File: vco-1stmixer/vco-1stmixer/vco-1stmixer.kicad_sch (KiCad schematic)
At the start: 51 parts, among them J101 VCO Control In, J102 1st IF Out, J103 VCO Sample, J104 RF In, J105 Conn_01x02, U101 POS-200, U102 MAV-11, U103 MAV-11, U104 TUF-1H+

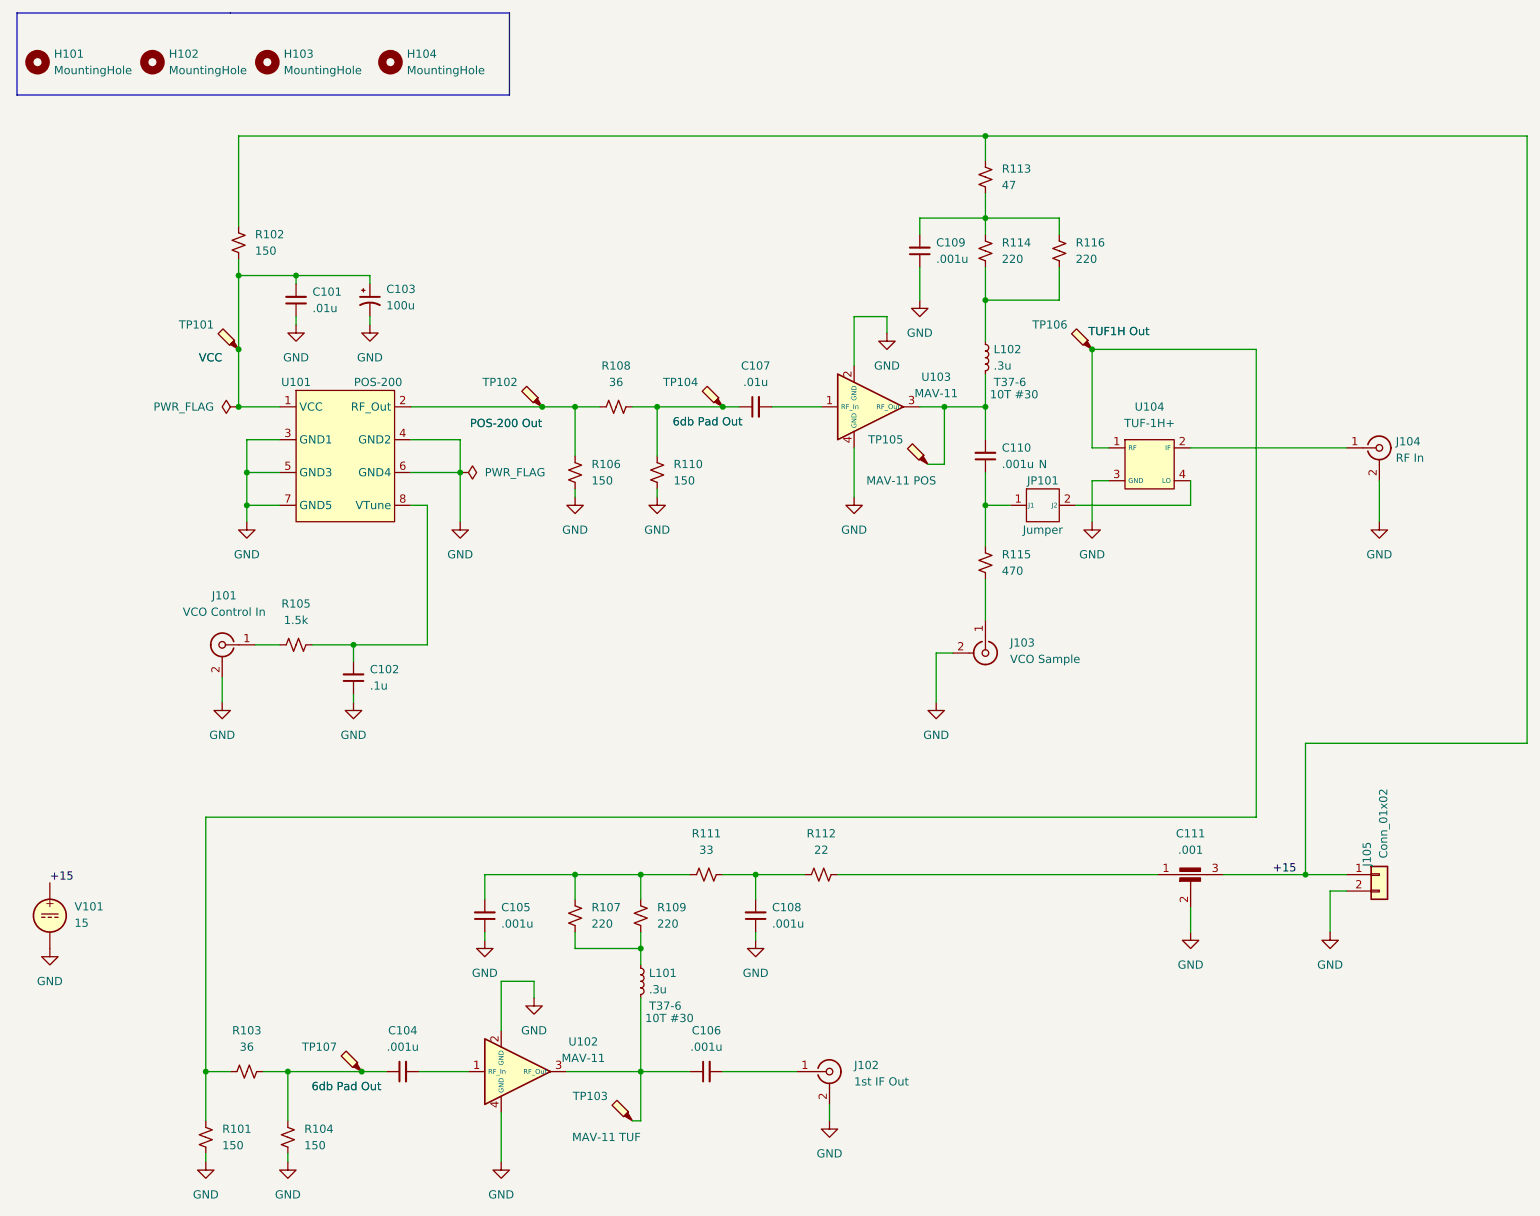
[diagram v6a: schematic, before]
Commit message: updates to 1st vco mixer to add some 3D Models
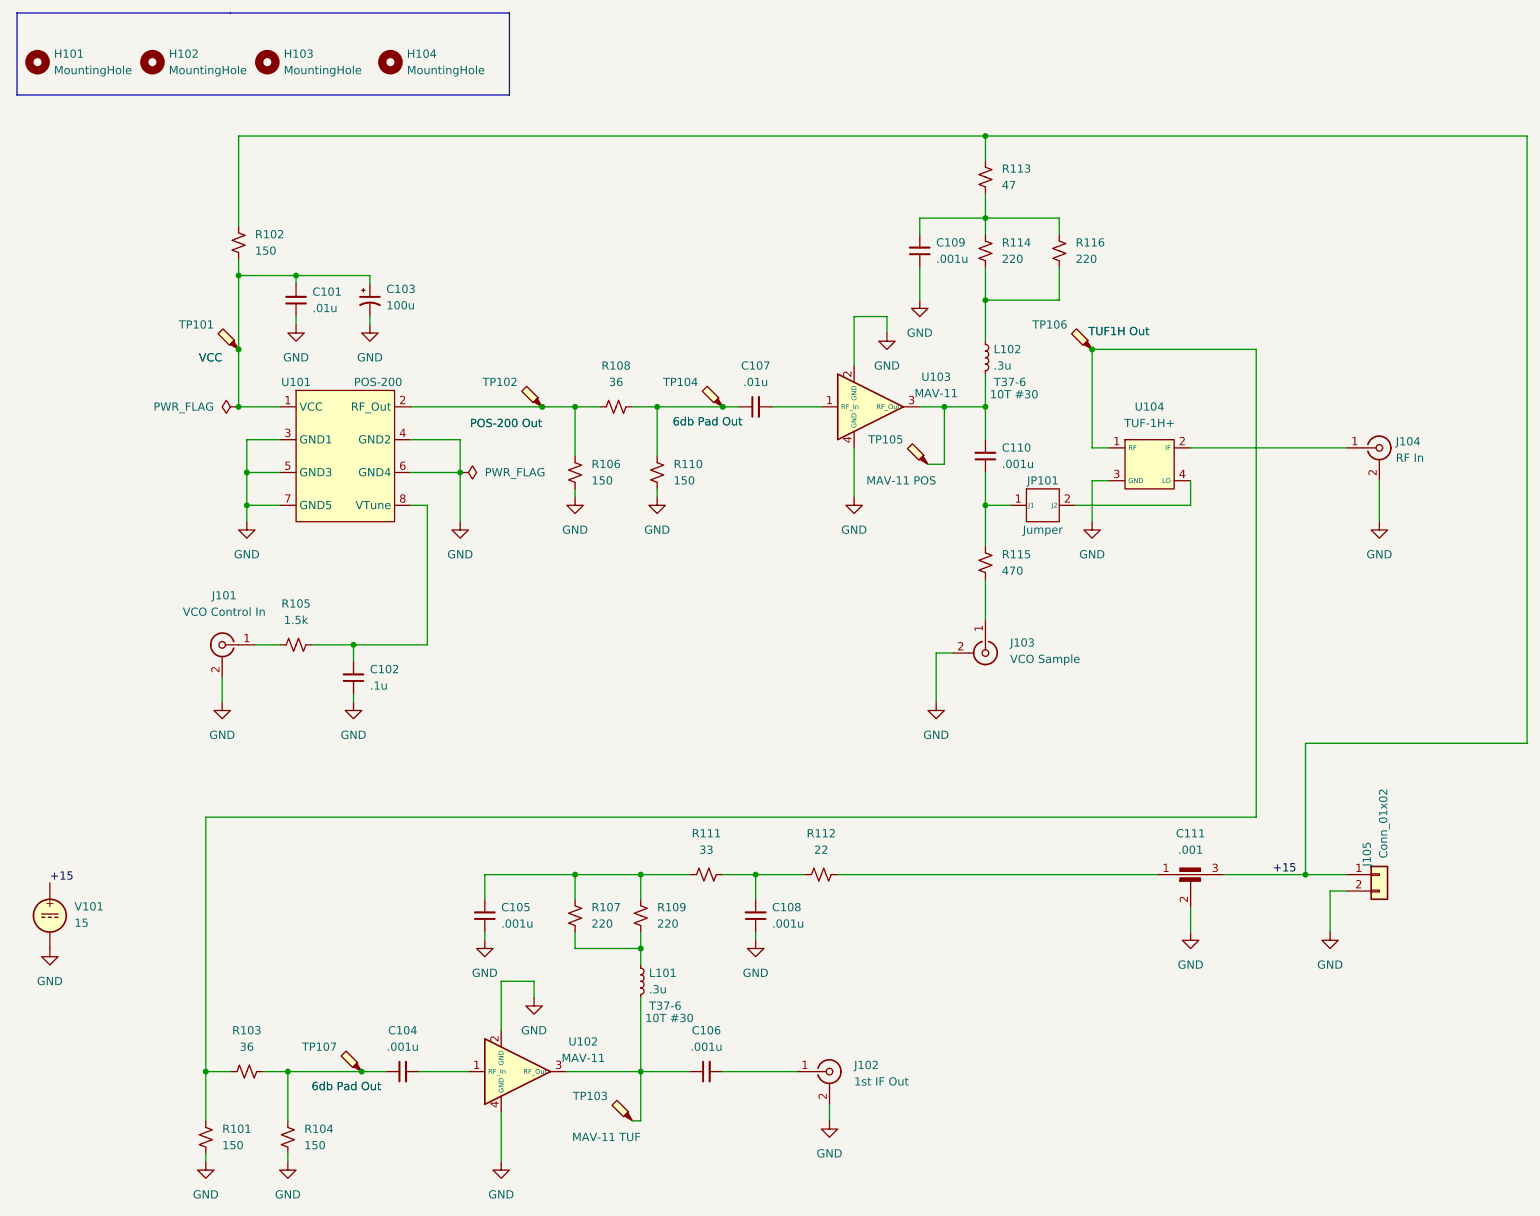
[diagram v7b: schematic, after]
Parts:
- JP101: Spice_Netlist_Enabled N -> (none)
